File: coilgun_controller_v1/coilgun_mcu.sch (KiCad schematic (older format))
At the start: 32 parts, among them J1 Conn_01x08, J2 Conn_01x05, J3 400V_GENERATOR_VIN, J4 BAT_IN, J5 3V3PWR, J6 3V3, J7 Conn_02x04_Odd_Even, J8 Conn_01x08, SW1 SW_TRIGGER_CHARGE, SW2 SW_TRIGGER_FIRE, SW3 SW_SAFETY, U1 STM32F072CBTx, U2 TLP185, U3 SPAN02A-03, U4 AMSRI-78-NZ, U5 TLP291-4, U6 TLP291-4

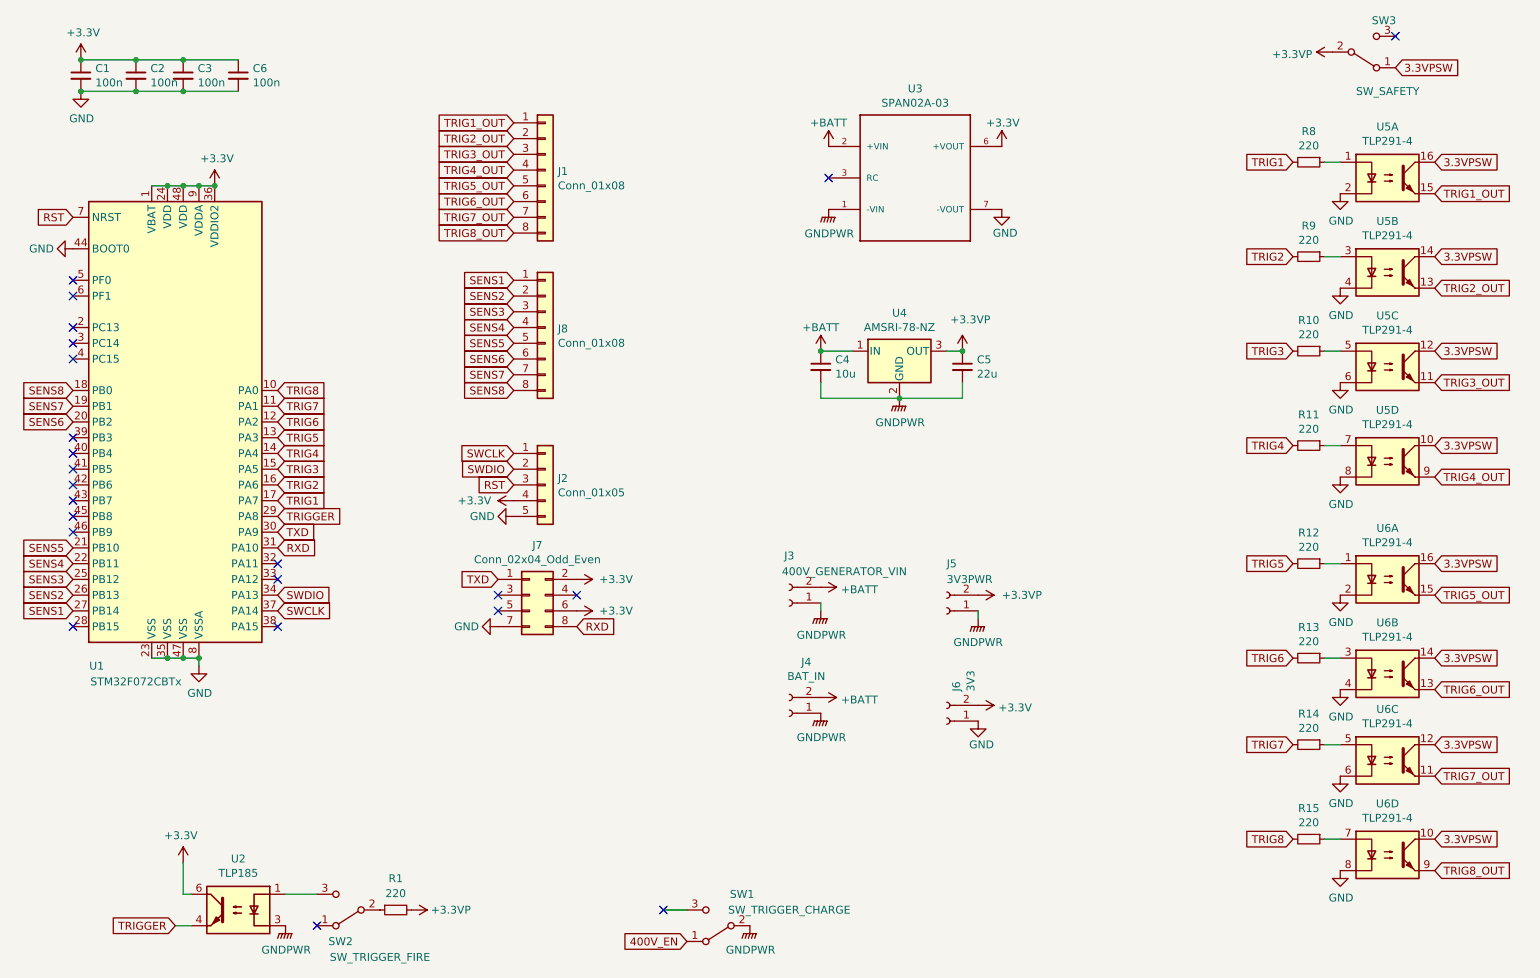
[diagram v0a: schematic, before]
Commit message: Increase track clearance, cosmetic fixes
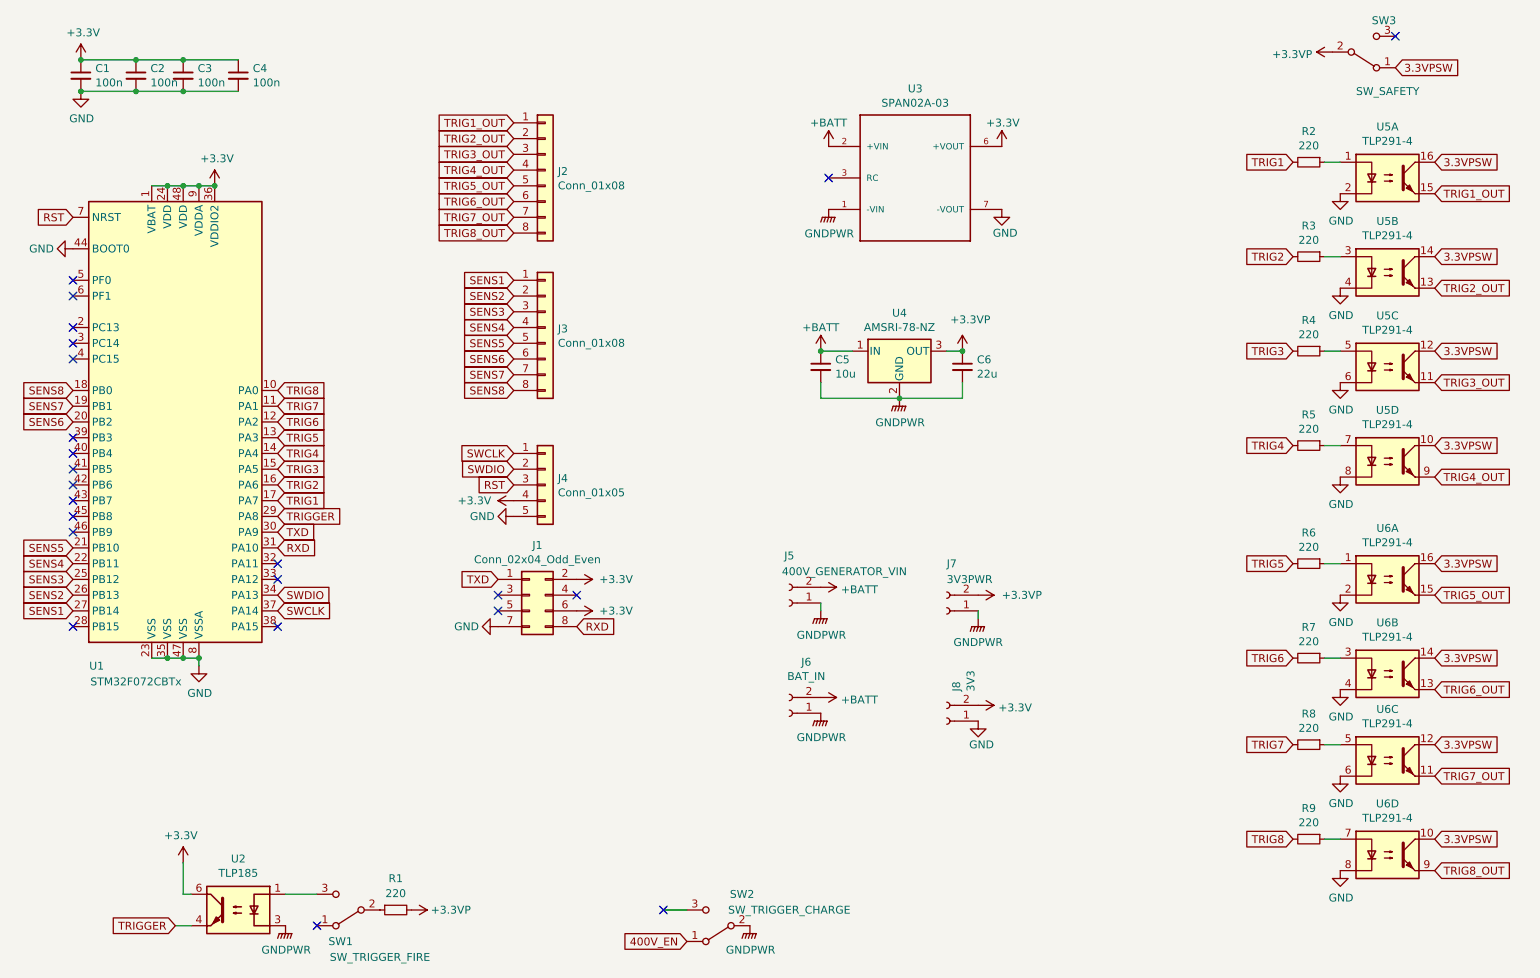
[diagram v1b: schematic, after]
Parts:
- renumbered C6 to C4, C4 to C5, C5 to C6, J7 to J1, J1 to J2, J8 to J3, J2 to J4, J3 to J5, J4 to J6, J5 to J7, J6 to J8, R8 to R2, R9 to R3, R10 to R4, R11 to R5, R12 to R6, R13 to R7, R14 to R8, R15 to R9, SW2 to SW1, SW1 to SW2

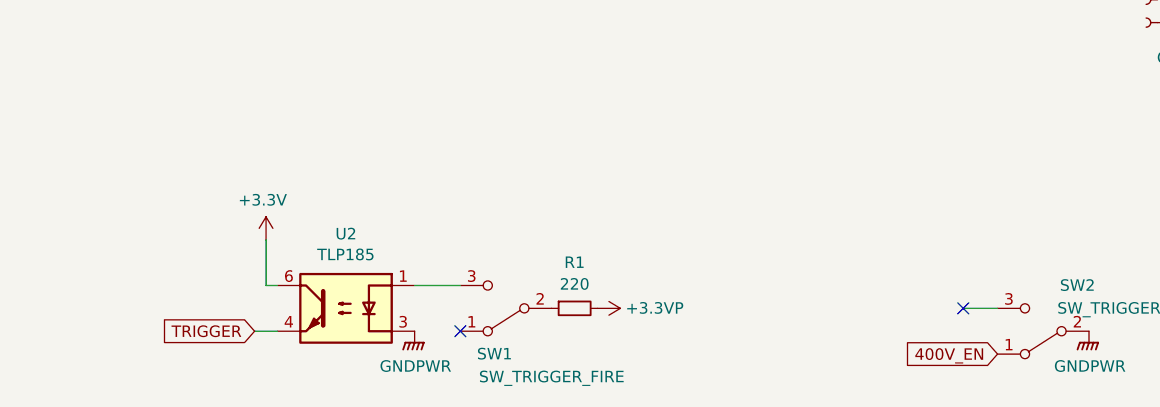
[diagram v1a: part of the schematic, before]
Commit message: Get rid of the useless optocoupler
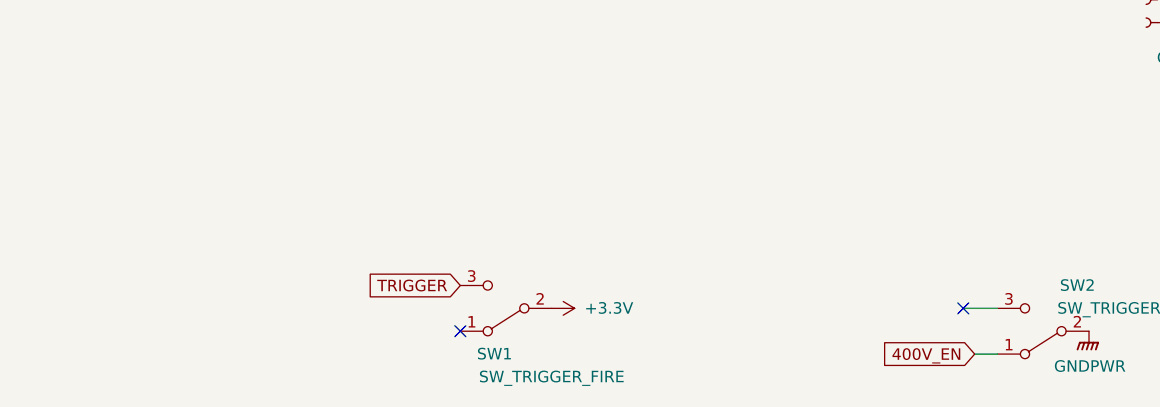
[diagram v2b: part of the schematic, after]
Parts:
- removed R1: 220, Resistor_SMD:R_0201_0603Metric_Pad0.64x0.40mm_HandSolder, symbol Device:R_Small
- removed U2: TLP185, Package_SO:SOIC-4_4.55x3.7mm_P2.54mm, symbol Isolator:TLP185
- C1, C2, C3, C4: footprint Capacitor_SMD:C_0201_0603Metric_Pad0.64x0.40mm_HandSolder -> Capacitor_SMD:C_0603_1608Metric_Pad1.08x0.95mm_HandSolder
- R2, R3, R4, R5, R6, R7, R8, R9: footprint Resistor_SMD:R_0201_0603Metric_Pad0.64x0.40mm_HandSolder -> Resistor_SMD:R_0603_1608Metric_Pad0.98x0.95mm_HandSolder
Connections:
- net +3V3: now also SW1.2 (B)
- net TRIGGER: now also SW1.3 (C)
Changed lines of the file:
@@
 Comment4 ""
 $EndDescr
-$Comp
-L Isolator:TLP185 U2
-U 1 1 60A90ED6
-P 2150 6350
-F 0 "U2" H 2150 6675 50  0000 C CNN
-F 1 "TLP185" H 2150 6584 50  0000 C CNN
-F 2 "Package_SO:SOIC-4_4.55x3.7mm_P2.54mm" H 2150 6050 50  0001 C CIN
-F 3 "https://toshiba.semicon-storage.com/info/docget.jsp?did=11791&prodName=TLP185" H 2150 6350 50  0001 L CNN
-	1    2150 6350
-	-1   0    0    -1
-$EndComp
-Wire Wire Line
-	1800 6250 1850 6250
-Text GLabel 1750 6450 0    50   Input ~ 0
+Text GLabel 2650 6250 0    50   Input ~ 0
 TRIGGER
-Wire Wire Line
-	1750 6450 1850 6450
-Wire Wire Line
-	1800 6050 1800 6250
 Text GLabel 2400 3850 2    50   Input ~ 0
 TRIGGER
@@
 F 0 "C2" H 1592 1096 50  0000 L CNN
 F 1 "100n" H 1592 1005 50  0000 L CNN
-F 2 "Capacitor_SMD:C_0201_0603Metric_Pad0.64x0.40mm_HandSolder" H 1500 1050 50  0001 C CNN
+F 2 "Capacitor_SMD:C_0603_1608Metric_Pad1.08x0.95mm_HandSolder" H 1500 1050 50  0001 C CNN
 F 3 "~" H 1500 1050 50  0001 C CNN
 	1    1500 1050
@@
 F 0 "C3" H 1892 1096 50  0000 L CNN
 F 1 "100n" H 1892 1005 50  0000 L CNN
-F 2 "Capacitor_SMD:C_0201_0603Metric_Pad0.64x0.40mm_HandSolder" H 1800 1050 50  0001 C CNN
+F 2 "Capacitor_SMD:C_0603_1608Metric_Pad1.08x0.95mm_HandSolder" H 1800 1050 50  0001 C CNN
 F 3 "~" H 1800 1050 50  0001 C CNN
 	1    1800 1050
@@
 $EndComp
 $Comp
-L power:+3.3V #PWR04
-U 1 1 60BBFBF4
-P 1800 6050
-F 0 "#PWR04" H 1800 5900 50  0001 C CNN
-F 1 "+3.3V" H 1815 6223 50  0000 C CNN
-F 2 "" H 1800 6050 50  0001 C CNN
-F 3 "" H 1800 6050 50  0001 C CNN
-	1    1800 6050
-	-1   0    0    -1
-$EndComp
-$Comp
 L Connector:Conn_01x02_Female J8
 U 1 1 60BCC328
@@
 	1    0    0    -1
 $EndComp
-Text GLabel 5000 6550 0    50   Input ~ 0
+Text GLabel 4900 6550 0    50   Input ~ 0
 400V_EN
 Text GLabel 1100 4150 0    50   Input ~ 0
@@
 F 0 "C1" H 1242 1096 50  0000 L CNN
 F 1 "100n" H 1242 1005 50  0000 L CNN
-F 2 "Capacitor_SMD:C_0201_0603Metric_Pad0.64x0.40mm_HandSolder" H 1150 1050 50  0001 C CNN
+F 2 "Capacitor_SMD:C_0603_1608Metric_Pad1.08x0.95mm_HandSolder" H 1150 1050 50  0001 C CNN
 F 3 "~" H 1150 1050 50  0001 C CNN
 	1    1150 1050
@@
 F 0 "R2" V 8754 1600 50  0000 C CNN
 F 1 "220" V 8845 1600 50  0000 C CNN
-F 2 "Resistor_SMD:R_0201_0603Metric_Pad0.64x0.40mm_HandSolder" H 8950 1600 50  0001 C CNN
+F 2 "Resistor_SMD:R_0603_1608Metric_Pad0.98x0.95mm_HandSolder" H 8950 1600 50  0001 C CNN
 F 3 "~" H 8950 1600 50  0001 C CNN
 	1    8950 1600
@@
 F 0 "R3" V 8754 2200 50  0000 C CNN
 F 1 "220" V 8845 2200 50  0000 C CNN
-F 2 "Resistor_SMD:R_0201_0603Metric_Pad0.64x0.40mm_HandSolder" H 8950 2200 50  0001 C CNN
+F 2 "Resistor_SMD:R_0603_1608Metric_Pad0.98x0.95mm_HandSolder" H 8950 2200 50  0001 C CNN
 F 3 "~" H 8950 2200 50  0001 C CNN
 	1    8950 2200
@@
 F 0 "R4" V 8754 2800 50  0000 C CNN
 F 1 "220" V 8845 2800 50  0000 C CNN
-F 2 "Resistor_SMD:R_0201_0603Metric_Pad0.64x0.40mm_HandSolder" H 8950 2800 50  0001 C CNN
+F 2 "Resistor_SMD:R_0603_1608Metric_Pad0.98x0.95mm_HandSolder" H 8950 2800 50  0001 C CNN
 F 3 "~" H 8950 2800 50  0001 C CNN
 	1    8950 2800
@@
 F 0 "R5" V 8754 3400 50  0000 C CNN
 F 1 "220" V 8845 3400 50  0000 C CNN
-F 2 "Resistor_SMD:R_0201_0603Metric_Pad0.64x0.40mm_HandSolder" H 8950 3400 50  0001 C CNN
+F 2 "Resistor_SMD:R_0603_1608Metric_Pad0.98x0.95mm_HandSolder" H 8950 3400 50  0001 C CNN
 F 3 "~" H 8950 3400 50  0001 C CNN
 	1    8950 3400
@@
 F 0 "R6" V 8754 4150 50  0000 C CNN
 F 1 "220" V 8845 4150 50  0000 C CNN
-F 2 "Resistor_SMD:R_0201_0603Metric_Pad0.64x0.40mm_HandSolder" H 8950 4150 50  0001 C CNN
+F 2 "Resistor_SMD:R_0603_1608Metric_Pad0.98x0.95mm_HandSolder" H 8950 4150 50  0001 C CNN
 F 3 "~" H 8950 4150 50  0001 C CNN
 	1    8950 4150
@@
 F 0 "R7" V 8754 4750 50  0000 C CNN
 F 1 "220" V 8845 4750 50  0000 C CNN
-F 2 "Resistor_SMD:R_0201_0603Metric_Pad0.64x0.40mm_HandSolder" H 8950 4750 50  0001 C CNN
+F 2 "Resistor_SMD:R_0603_1608Metric_Pad0.98x0.95mm_HandSolder" H 8950 4750 50  0001 C CNN
 F 3 "~" H 8950 4750 50  0001 C CNN
 	1    8950 4750
@@
 F 0 "R8" V 8754 5300 50  0000 C CNN
 F 1 "220" V 8845 5300 50  0000 C CNN
-F 2 "Resistor_SMD:R_0201_0603Metric_Pad0.64x0.40mm_HandSolder" H 8950 5300 50  0001 C CNN
+F 2 "Resistor_SMD:R_0603_1608Metric_Pad0.98x0.95mm_HandSolder" H 8950 5300 50  0001 C CNN
 F 3 "~" H 8950 5300 50  0001 C CNN
 	1    8950 5300
@@
 F 0 "R9" V 8754 5900 50  0000 C CNN
 F 1 "220" V 8845 5900 50  0000 C CNN
-F 2 "Resistor_SMD:R_0201_0603Metric_Pad0.64x0.40mm_HandSolder" H 8950 5900 50  0001 C CNN
+F 2 "Resistor_SMD:R_0603_1608Metric_Pad0.98x0.95mm_HandSolder" H 8950 5900 50  0001 C CNN
 F 3 "~" H 8950 5900 50  0001 C CNN
 	1    8950 5900
@@
 	1    0    0    1
 $EndComp
-$Comp
-L power:+3.3VP #PWR08
-U 1 1 60A9CDAD
-P 3250 6350
-F 0 "#PWR08" H 3400 6300 50  0001 C CNN
-F 1 "+3.3VP" V 3250 6600 50  0000 C CNN
-F 2 "" H 3250 6350 50  0001 C CNN
-F 3 "" H 3250 6350 50  0001 C CNN
-	1    3250 6350
-	0    1    -1   0
-$EndComp
-$Comp
-L Device:R_Small R1
-U 1 1 60B829F7
-P 3150 6350
-F 0 "R1" V 2950 6350 50  0000 C CNN
-F 1 "220" V 3045 6350 50  0000 C CNN
-F 2 "Resistor_SMD:R_0201_0603Metric_Pad0.64x0.40mm_HandSolder" H 3150 6350 50  0001 C CNN
-F 3 "~" H 3150 6350 50  0001 C CNN
-	1    3150 6350
-	0    -1   1    0
-$EndComp
 Wire Wire Line
 	4850 6350 5000 6350
-Wire Wire Line
-	2450 6250 2650 6250
-$Comp
-L power:GNDPWR #PWR07
-U 1 1 60AAE7A4
-P 2450 6450
-F 0 "#PWR07" H 2450 6250 50  0001 C CNN
-F 1 "GNDPWR" H 2454 6296 50  0000 C CNN
-F 2 "" H 2450 6400 50  0001 C CNN
-F 3 "" H 2450 6400 50  0001 C CNN
-	1    2450 6450
-	1    0    0    -1
-$EndComp
 $Comp
 L power:+3.3VP #PWR030
@@
 F 0 "C4" H 2242 1096 50  0000 L CNN
 F 1 "100n" H 2242 1005 50  0000 L CNN
-F 2 "Capacitor_SMD:C_0201_0603Metric_Pad0.64x0.40mm_HandSolder" H 2150 1050 50  0001 C CNN
+F 2 "Capacitor_SMD:C_0603_1608Metric_Pad1.08x0.95mm_HandSolder" H 2150 1050 50  0001 C CNN
 F 3 "~" H 2150 1050 50  0001 C CNN
 	1    2150 1050
@@
 	-1   0    0    1
 $EndComp
+$Comp
+L power:+3.3V #PWR0101
+U 1 1 60D65D61
+P 3050 6350
+F 0 "#PWR0101" H 3050 6200 50  0001 C CNN
+F 1 "+3.3V" V 3050 6600 50  0000 C CNN
+F 2 "" H 3050 6350 50  0001 C CNN
+F 3 "" H 3050 6350 50  0001 C CNN
+	1    3050 6350
+	0    1    1    0
+$EndComp
+Wire Wire Line
+	4900 6550 5000 6550
 $EndSCHEMATC
